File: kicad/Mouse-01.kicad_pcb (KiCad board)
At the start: 2 copper layers, 74 x 72 mm, 91 parts, among them P1 MT-ENC, P2 MT-ENC, P3 Battery_A, P4 Battery_B, P5 SWD, P6 UART, Q1 IRFML8244, Q2 IRFML8244, Q3 BSS138, SW1 RESET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

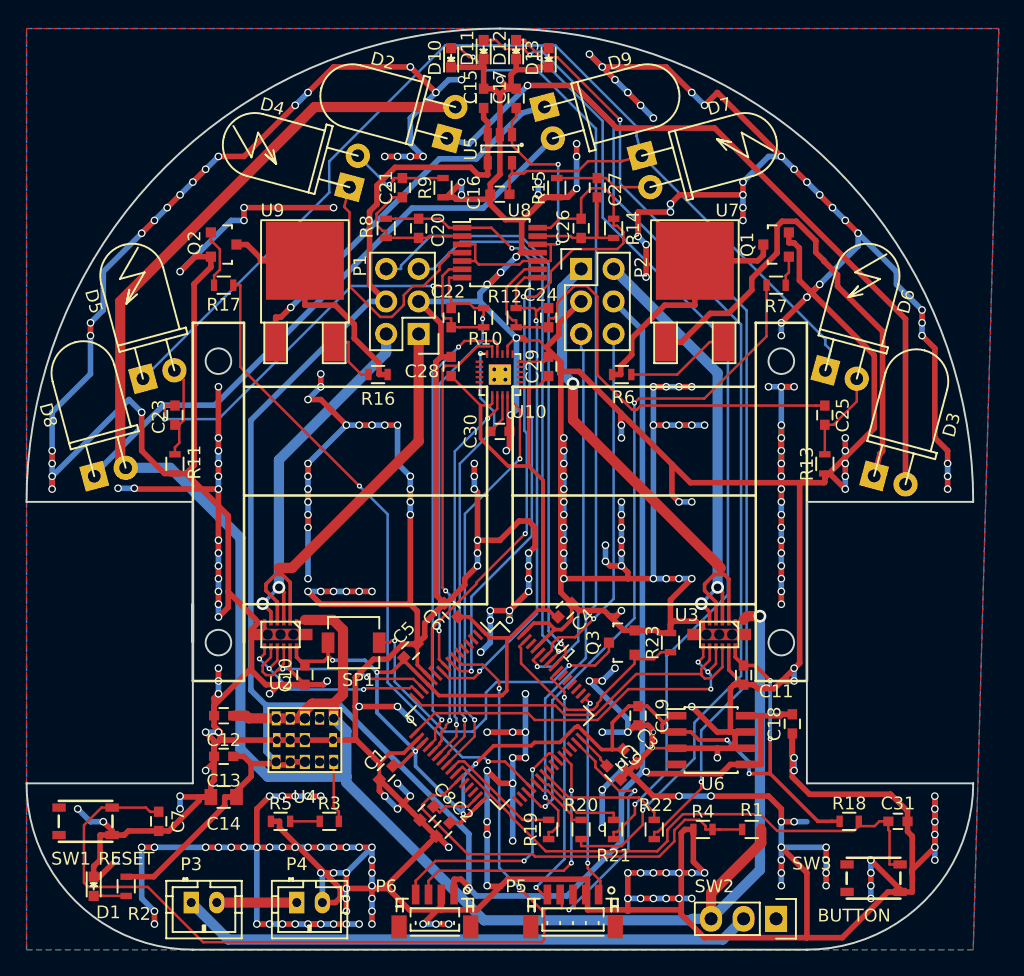
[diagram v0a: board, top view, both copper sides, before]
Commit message: ベタグランドの修正
モータードライバの放熱効果を高めるために，サーマルリリーフをやめてベタ接続に．
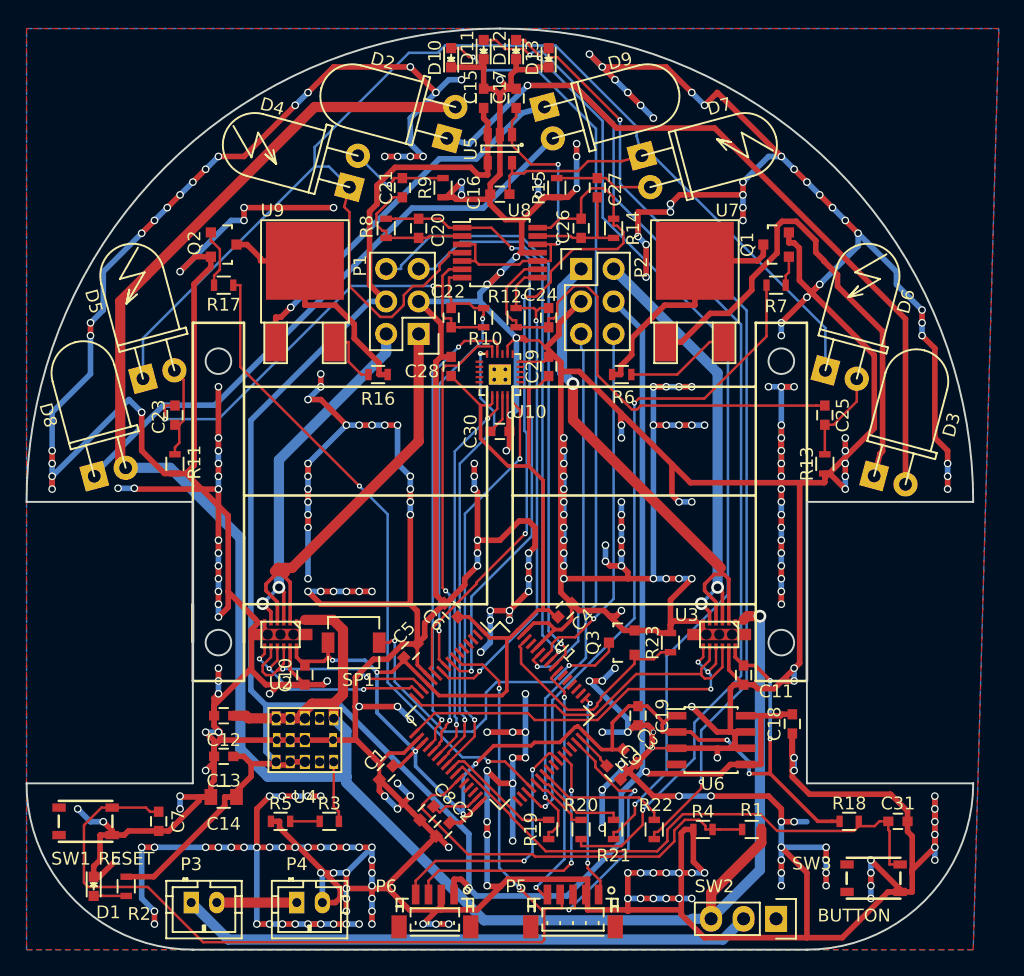
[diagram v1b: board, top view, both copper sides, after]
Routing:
- net +3.3VADC: track 114.1 -> 117.5 mm
- net /Motor_L/MT_OUT_1: track 32.9 -> 33.8 mm
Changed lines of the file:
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@@
     (thickness 1)
     (drawings 54)
-    (tracks 2071)
+    (tracks 2077)
     (zones 0)
     (modules 91)
@@
     (pcbplotparams
       (layerselection 0x010f0_80000001)
-      (usegerberextensions false)
+      (usegerberextensions true)
       (excludeedgelayer true)
       (linewidth 0.100000)
@@
       (drillshape 0)
       (scaleselection 1)
-      (outputdirectory ""))
+      (outputdirectory elecrow/))
   )
   (net 0 "")
@@
   (gr_line (start 119 110) (end 119 88) (angle 90) (layer Edge.Cuts) (width 0.15))
   (gr_line (start 167 110) (end 167 88) (angle 90) (layer Edge.Cuts) (width 0.15))
+  (segment (start 129.6617 62.9735) (end 129.6616 62.9734) (width 0.2) (layer B.Cu) (net 0))
+  (segment (start 129.6616 62.9734) (end 129.6617 62.9735) (width 0.2) (layer B.Cu) (net 0))
   (via (at 160.7617 106.6094) (size 0.4) (layers F.Cu B.Cu) (net 1))
   (via (at 133.393 101.3175) (size 0.4) (layers F.Cu B.Cu) (net 1))
@@
   (segment (start 134.6406 108.63) (end 135.196 108.63) (width 0.29) (layer F.Cu) (net 1))
   (segment (start 134.6406 108.63) (end 134.6403 108.6297) (width 0.29) (layer F.Cu) (net 1))
-  (segment (start 111.25 117.3007) (end 111.6993 117.3007) (width 0.44) (layer F.Cu) (net 2) (status 400000))
+  (segment (start 111.25 117.3007) (end 111.6993 117.3007) (width 0.44) (layer F.Cu) (net 2))
   (via (at 113 116) (size 0.6) (drill 0.4) (layers F.Cu B.Cu) (net 2))
   (segment (start 111.6993 117.3007) (end 113 116) (width 0.44) (layer F.Cu) (net 2))
@@
   (segment (start 133 120) (end 133 121) (width 0.44) (layer F.Cu) (net 2))
   (via (at 133 121) (size 0.6) (drill 0.4) (layers F.Cu B.Cu) (net 2))
-  (segment (start 129.125 119.32) (end 129.125 117.125) (width 0.44) (layer B.Cu) (net 2) (status 400000))
+  (segment (start 129.125 119.32) (end 129.125 117.125) (width 0.44) (layer B.Cu) (net 2))
   (via (at 131 120) (size 0.6) (drill 0.4) (layers F.Cu B.Cu) (net 2))
   (segment (start 131 119) (end 131 120) (width 0.44) (layer F.Cu) (net 2))
@@
   (segment (start 134.11 72.33) (end 132.8092 71.0292) (width 0.44) (layer F.Cu) (net 7))
   (segment (start 142.05 61.492) (end 142.05 62.4423) (width 0.44) (layer F.Cu) (net 7))
+  (segment (start 168.443274 77.7163) (end 168.443274 74.405274) (width 0.2) (layer B.Cu) (net 8))
+  (segment (start 168.443274 74.405274) (end 154.981274 60.943274) (width 0.2) (layer B.Cu) (net 8))
+  (segment (start 154.981274 60.943274) (end 154.1013 60.943274) (width 0.2) (layer B.Cu) (net 8))
+  (segment (start 128.522 61.789) (end 129.633574 61.789) (width 0.2) (layer B.Cu) (net 8))
+  (segment (start 129.633574 61.789) (end 131.2413 63.396726) (width 0.2) (layer B.Cu) (net 8))
+  (segment (start 115.103274 78.3737) (end 115.103274 75.207726) (width 0.2) (layer B.Cu) (net 8))
+  (segment (start 138.1468 52.899) (end 138.7179 52.3279) (width 0.2) (layer B.Cu) (net 8))
+  (segment (start 135.888 52.899) (end 138.1468 52.899) (width 0.2) (layer B.Cu) (net 8))
+  (segment (start 128.522 60.265) (end 135.888 52.899) (width 0.2) (layer B.Cu) (net 8))
+  (segment (start 128.522 61.789) (end 128.522 60.265) (width 0.2) (layer B.Cu) (net 8))
+  (segment (start 115.103274 75.207726) (end 128.522 61.789) (width 0.2) (layer B.Cu) (net 8))
   (segment (start 143.75 63.948) (end 143.75 63.2727) (width 0.2) (layer F.Cu) (net 8))
-  (segment (start 168.4433 77.7163) (end 168.8666 76.1366) (width 0.2) (layer B.Cu) (net 8))
   (segment (start 143.95 61.492) (end 143.95 62.3223) (width 0.2) (layer F.Cu) (net 8))
   (segment (start 144.8782 62.3223) (end 143.95 62.3223) (width 0.2) (layer F.Cu) (net 8))
@@
   (segment (start 152.5216 61.3666) (end 152.5216 61.3665) (width 0.2) (layer F.Cu) (net 8))
   (segment (start 154.1013 60.9433) (end 152.5216 61.3666) (width 0.2) (layer F.Cu) (net 8))
-  (segment (start 129.6616 63.8154) (end 129.6616 62.9734) (width 0.2) (layer B.Cu) (net 8))
-  (segment (start 115.1033 78.3737) (end 129.6616 63.8154) (width 0.2) (layer B.Cu) (net 8))
   (segment (start 143.75 62.5223) (end 143.75 63.2727) (width 0.2) (layer F.Cu) (net 8))
   (segment (start 143.95 62.3223) (end 143.75 62.5223) (width 0.2) (layer F.Cu) (net 8))
-  (segment (start 168.4433 75.2853) (end 154.1013 60.9433) (width 0.2) (layer B.Cu) (net 8))
-  (segment (start 168.4433 75.7134) (end 168.4433 75.2853) (width 0.2) (layer B.Cu) (net 8))
-  (segment (start 168.8665 76.1366) (end 168.4433 75.7134) (width 0.2) (layer B.Cu) (net 8))
-  (segment (start 168.8666 76.1366) (end 168.8665 76.1366) (width 0.2) (layer B.Cu) (net 8))
   (segment (start 154.1013 60.9433) (end 153.6875 59.3989) (width 0.2) (layer B.Cu) (net 8))
-  (segment (start 129.6617 62.9735) (end 129.6616 62.9734) (width 0.2) (layer B.Cu) (net 8))
-  (segment (start 131.2413 63.3967) (end 129.6617 62.9735) (width 0.2) (layer B.Cu) (net 8))
   (segment (start 139.0247 68.7447) (end 139.0247 68.52) (width 0.2) (layer F.Cu) (net 8))
   (segment (start 138.2777 69.4917) (end 139.0247 68.7447) (width 0.2) (layer F.Cu) (net 8))
@@
   (segment (start 131.2413 63.3967) (end 130.8275 64.9411) (width 0.2) (layer F.Cu) (net 8))
   (segment (start 140.05 68.52) (end 139.0247 68.52) (width 0.2) (layer F.Cu) (net 8))
-  (segment (start 129.6616 62.9734) (end 129.6617 62.9735) (width 0.2) (layer B.Cu) (net 8))
-  (segment (start 129.6616 61.3842) (end 129.6616 62.9734) (width 0.2) (layer B.Cu) (net 8))
-  (segment (start 138.7179 52.3279) (end 129.6616 61.3842) (width 0.2) (layer B.Cu) (net 8))
   (segment (start 147.351 52.3279) (end 138.7179 52.3279) (width 0.2) (layer B.Cu) (net 8))
   (segment (start 153.6875 58.6644) (end 147.351 52.3279) (width 0.2) (layer B.Cu) (net 8))
@@
   (segment (start 146.1303 53.1569) (end 144.9691 51.9957) (width 0.2) (layer F.Cu) (net 26))
   (segment (start 146.1303 53.3227) (end 146.1303 53.1569) (width 0.2) (layer F.Cu) (net 26))
+  (segment (start 126.1725 93.539) (end 126.1725 93.158) (width 0.8) (layer F.Cu) (net 27))
+  (segment (start 125.7915 93.158) (end 126.1725 93.539) (width 0.8) (layer F.Cu) (net 27))
+  (segment (start 125.728 93.158) (end 125.7915 93.158) (width 0.8) (layer F.Cu) (net 27))
+  (segment (start 126.1725 93.158) (end 126.7535 93.158) (width 0.8) (layer F.Cu) (net 27))
+  (segment (start 125.6645 93.158) (end 125.4105 93.412) (width 0.8) (layer F.Cu) (net 27))
+  (segment (start 125.728 93.158) (end 125.6645 93.158) (width 0.8) (layer F.Cu) (net 27))
   (segment (start 125.474 93.666) (end 125.728 93.666) (width 0.29) (layer F.Cu) (net 27))
   (segment (start 124.712 94.428) (end 125.474 93.666) (width 0.29) (layer F.Cu) (net 27))
@@
   (segment (start 136.65 83.2615) (end 136.65 74.87) (width 0.8) (layer F.Cu) (net 27))
   (segment (start 126.7535 93.158) (end 136.65 83.2615) (width 0.8) (layer F.Cu) (net 27))
-  (segment (start 125.728 93.158) (end 126.7535 93.158) (width 0.8) (layer F.Cu) (net 27))
   (via (at 125.728 94.682) (size 1) (drill 0.6) (layers F.Cu B.Cu) (net 28))
   (via (at 124.458 95.952) (size 1) (drill 0.6) (layers F.Cu B.Cu) (net 28))
@@
   (segment (start 132.725 78.045) (end 132.1747 78.045) (width 0.2) (layer F.Cu) (net 73))
   (zone (net 2) (net_name GND) (layer F.Cu) (hatch edge 0.508)
-    (connect_pads (clearance 0.254))
+    (connect_pads yes (clearance 0.254))
     (min_thickness 0.254)
     (fill yes (arc_segments 16) (thermal_gap 0.508) (thermal_bridge_width 0.508))
@@
   )
   (zone (net 2) (net_name GND) (layer B.Cu) (hatch edge 0.508)
-    (connect_pads (clearance 0.254))
+    (connect_pads yes (clearance 0.254))
     (min_thickness 0.254)
     (fill yes (arc_segments 16) (thermal_gap 0.508) (thermal_bridge_width 0.508))
